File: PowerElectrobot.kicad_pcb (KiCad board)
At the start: 2 copper layers, 58 parts, among them J10 Conn_XT30F, J11 Conn_XT30F, J12 Conn_XT30F, J13 Conn_XT30F, J14 Conn_XT30F, J15 Conn_XT30F, J16 Conn_XT30F, J17 Conn_XT30F, J18 Conn_XT30F, J19 Conn_XT30F, J2 Conn_XT60M, J3 Conn_XT30F, J4 Conn_XT30F, J5 Conn_XT30F, J6 Conn_XT30F, J7 Conn_XT30F, J8 Conn_01x04, J9 Conn_01x04, Q1 BTS117, Q2 BTS117, Q3 BTS117, Q4 BTS117, Q5 BTS117, Q6 BTS117, Q7 BTS117, Q8 BTS117, U1 DSPIC33FJ128MC802-xSP, U2 TSR_2-2450, U3 MCP1804x-3302xDB, U4 ACS712xLCTR-05B, U5 ACS712xLCTR-05B, U6 ACS712xLCTR-20A

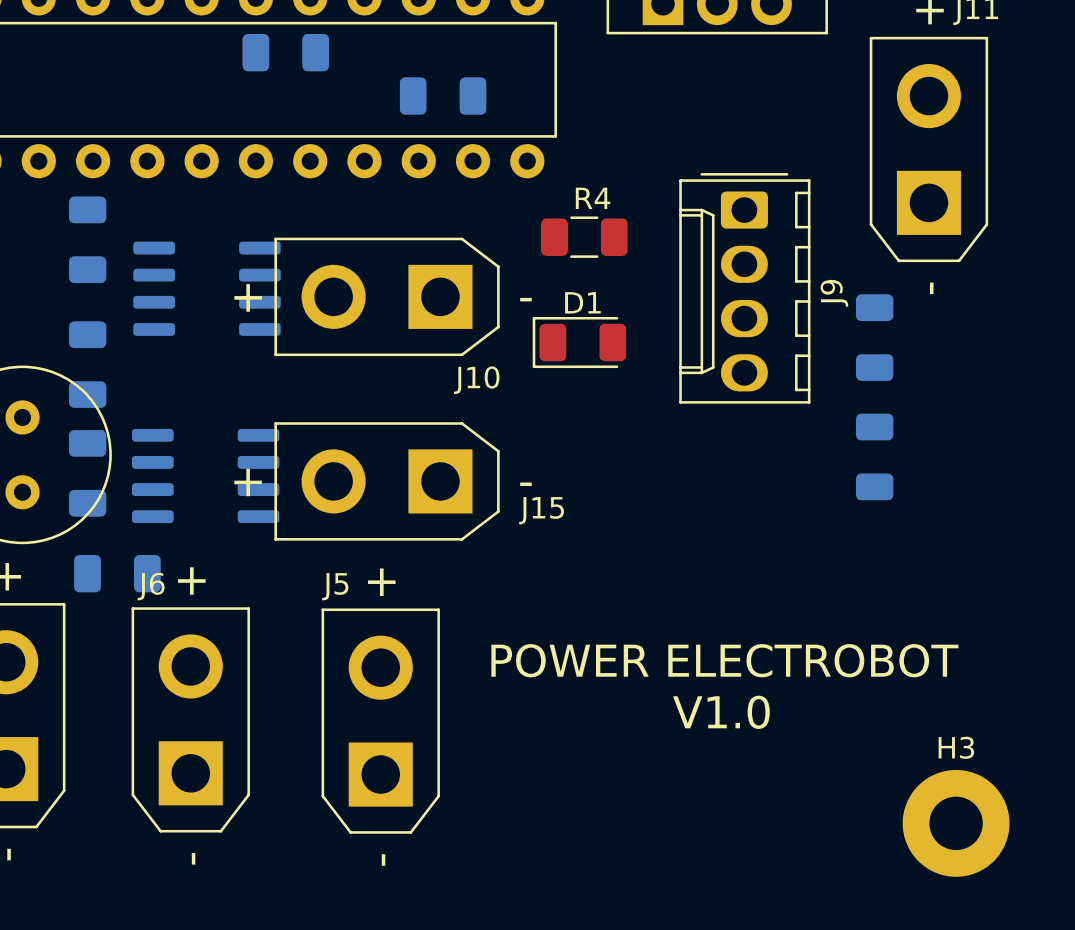
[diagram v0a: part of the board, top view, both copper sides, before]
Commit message: Création des via de 1.2mm
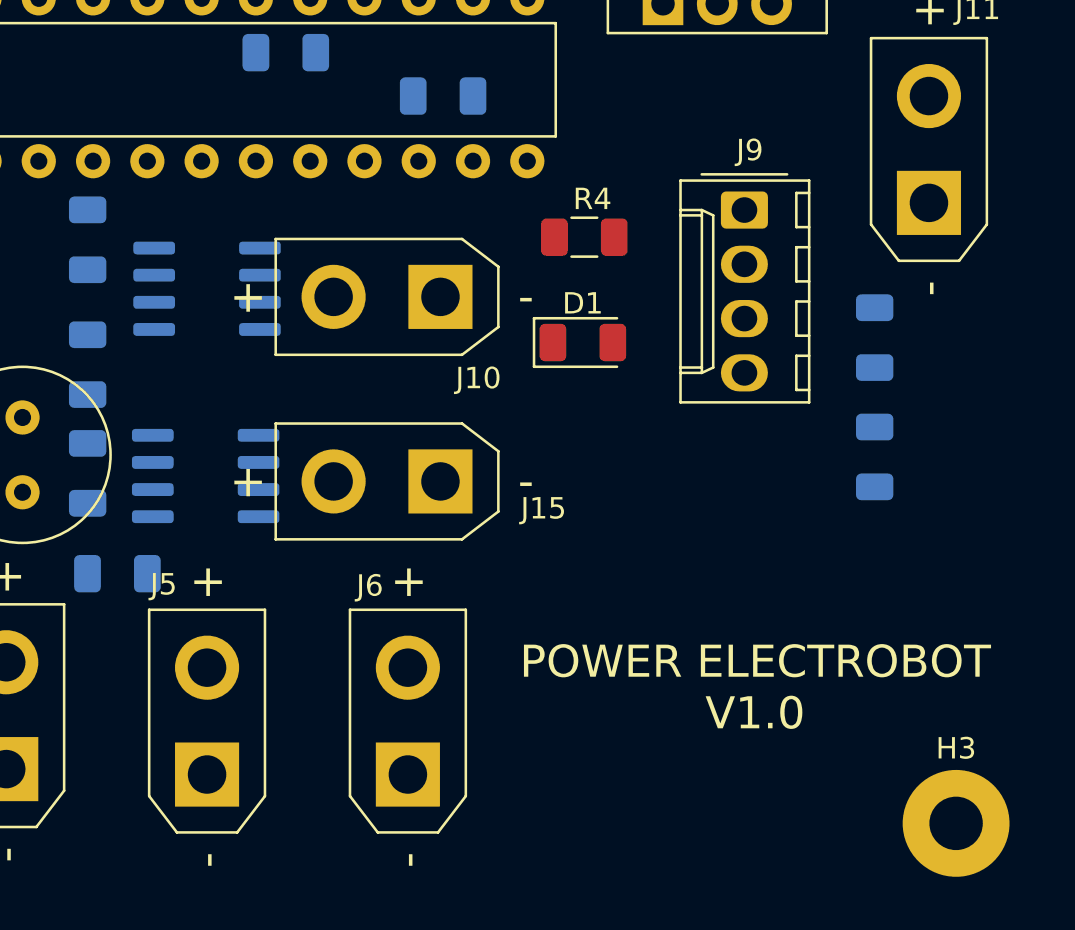
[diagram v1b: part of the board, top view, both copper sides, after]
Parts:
- moved J6 10.2 mm to (125.7, 117.6)
- moved J5 8.13 mm to (116.3, 117.6)
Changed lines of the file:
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@@
   )
   (setup
-    (last_trace_width 1.5)
+    (last_trace_width 0.25)
     (user_trace_width 0.5)
     (user_trace_width 0.75)
@@
     (user_trace_width 1.5)
     (user_trace_width 2)
+    (user_trace_width 2.5)
+    (user_trace_width 3)
     (trace_clearance 0.2)
     (zone_clearance 0.508)
@@
     (via_min_size 0.4)
     (via_min_drill 0.3)
+    (user_via 1.2 0.6)
     (uvia_size 0.3)
     (uvia_drill 0.1)
@@
   )
   (module XT30:AMASS_XT30UPB-F_1x02_P5.0mm_Vertical (layer F.Cu)
-    (at 124.46 117.602 90)
+    (at 116.332 117.602 90)
     (descr "Connector XT30 Vertical PCB Female, https://www.tme.eu/en/Document/4acc913878197f8c2e30d4b8cdc47230/XT30UPB%20SPEC.pdf")
     (tags "RC Connector XT30")
@@
   )
   (module XT30:AMASS_XT30UPB-F_1x02_P5.0mm_Vertical (layer F.Cu)
-    (at 115.57 117.545001 90)
+    (at 125.73 117.602 90)
     (descr "Connector XT30 Vertical PCB Female, https://www.tme.eu/en/Document/4acc913878197f8c2e30d4b8cdc47230/XT30UPB%20SPEC.pdf")
     (tags "RC Connector XT30")
@@
     (descr "Molex KK-254 Interconnect System, old/engineering part number: AE-6410-04A example for new part number: 22-27-2041, 4 Pins (http://www.molex.com/pdm_docs/sd/022272021_sd.pdf), generated with kicad-footprint-generator")
     (tags "connector Molex KK-254 side entry")
-    (fp_text reference J9 (at 3.81 -4.12 90) (layer F.SilkS)
+    (fp_text reference J9 (at -2.794 -0.254 180) (layer F.SilkS)
       (effects (font (size 1 1) (thickness 0.15)))
     )
@@
   (gr_circle (center 120.396 101.6) (end 120.523 101.6) (layer B.SilkS) (width 0.5))
   (gr_circle (center 120.396 92.964) (end 120.523 92.964) (layer B.SilkS) (width 0.5))
-  (gr_text "POWER ELECTROBOT\nV1.0" (at 140.462 113.538) (layer F.SilkS)
+  (gr_text "POWER ELECTROBOT\nV1.0" (at 141.986 113.538) (layer F.SilkS)
     (effects (font (size 1.5 1.5) (thickness 0.15)))
   )

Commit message: Début du routage de la carte
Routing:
- net /VBAT: track 0.00 -> 224.8 mm
- net +5V: track 0.00 -> 119.9 mm, vias 0 -> 2
- net GND: track 0.00 -> 90.1 mm, vias 0 -> 1
- net /3.3V_dsPIC: track 0.00 -> 87.9 mm, vias 0 -> 3
- net /MEAS_CURR_VBAT: track 0.00 -> 35.4 mm
- net Net-(J18-Pad1): track 0.00 -> 32.5 mm
- net Net-(J12-Pad1): track 0.00 -> 23.9 mm
- net /dsPIC_Stor8: track 0.00 -> 20.4 mm
- net Net-(J14-Pad1): track 0.00 -> 19.0 mm
- net /dsPIC_MCLR: track 0.00 -> 18.6 mm
- net Net-(J11-Pad1): track 0.00 -> 14.7 mm
- net /dsPIC_Stor7: track 0.00 -> 14.2 mm
- net /dsPIC_Stor2: track 0.00 -> 13.3 mm
- net Net-(J17-Pad1): track 0.00 -> 12.1 mm
- net Net-(J13-Pad1): track 0.00 -> 11.2 mm
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
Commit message: mise a jour pcb
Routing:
- net /dsPIC_PGED1: track 0.00 -> 23.1 mm, vias 0 -> 1
- net /VBAT: track 224.8 -> 239.1 mm
- net /MEAS_CURR_1: track 0.00 -> 11.0 mm
- net /I2C_SCL1: track 6.94 -> 17.6 mm, vias 0 -> 1
- net /VBAT_f: track 6.57 -> 15.7 mm
- net Net-(C10-Pad2): track 0.00 -> 3.74 mm
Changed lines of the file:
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@@
     (thickness 1.6)
     (drawings 3)
-    (tracks 266)
+    (tracks 297)
     (zones 0)
     (modules 58)
@@
   )
   (setup
-    (last_trace_width 0.75)
+    (last_trace_width 1)
     (user_trace_width 0.5)
     (user_trace_width 0.75)
@@
   (segment (start 103.124 92.514) (end 103.119001 92.509001) (width 0.75) (layer B.Cu) (net 3))
   (segment (start 103.124 95.25) (end 103.124 92.514) (width 0.75) (layer B.Cu) (net 3))
+  (segment (start 101.637999 88.100001) (end 100.838 88.9) (width 0.25) (layer B.Cu) (net 3))
+  (segment (start 101.963001 87.774999) (end 101.637999 88.100001) (width 0.25) (layer B.Cu) (net 3))
+  (segment (start 103.918001 87.774999) (end 101.963001 87.774999) (width 0.25) (layer B.Cu) (net 3))
+  (segment (start 104.503001 88.359999) (end 103.918001 87.774999) (width 0.25) (layer B.Cu) (net 3))
+  (segment (start 104.503001 90.305001) (end 104.503001 88.359999) (width 0.25) (layer B.Cu) (net 3))
+  (segment (start 103.119001 91.689001) (end 104.503001 90.305001) (width 0.25) (layer B.Cu) (net 3))
+  (segment (start 103.119001 92.509001) (end 103.119001 91.689001) (width 0.25) (layer B.Cu) (net 3))
   (segment (start 95.69171 85.15629) (end 94.996 85.852) (width 0.75) (layer B.Cu) (net 4))
   (segment (start 96.19201 84.65599) (end 95.69171 85.15629) (width 0.75) (layer B.Cu) (net 4))
@@
   (segment (start 116.332 112.602) (end 116.332 104.332) (width 0.75) (layer B.Cu) (net 5))
   (segment (start 116.332 104.332) (end 117.27201 103.39199) (width 0.75) (layer B.Cu) (net 5))
+  (segment (start 92.879999 97.261999) (end 97.431998 92.71) (width 1) (layer F.Cu) (net 5))
+  (segment (start 89.408 103.632) (end 92.879999 100.160001) (width 1) (layer F.Cu) (net 5))
+  (segment (start 92.879999 100.160001) (end 92.879999 97.261999) (width 1) (layer F.Cu) (net 5))
   (segment (start 106.56463 104.394) (end 107.696 104.394) (width 0.75) (layer B.Cu) (net 6))
   (segment (start 101.426 104.394) (end 106.56463 104.394) (width 0.75) (layer B.Cu) (net 6))
@@
   (segment (start 94.822 97.79) (end 99.822 102.79) (width 0.75) (layer F.Cu) (net 6))
   (segment (start 93.98 97.79) (end 94.822 97.79) (width 0.75) (layer F.Cu) (net 6))
+  (segment (start 112.262 95.504) (end 110.744 97.022) (width 0.25) (layer B.Cu) (net 7))
+  (segment (start 113.857 95.504) (end 112.262 95.504) (width 0.25) (layer B.Cu) (net 7))
   (segment (start 77.256195 108.585) (end 78.108 108.585) (width 0.75) (layer B.Cu) (net 9))
   (segment (start 78.108 108.585) (end 79.183 108.585) (width 0.75) (layer B.Cu) (net 9))
@@
   (segment (start 74.233 112.333) (end 76.708 114.808) (width 0.75) (layer B.Cu) (net 12))
   (segment (start 74.233 109.855) (end 74.233 112.333) (width 0.75) (layer B.Cu) (net 12))
+  (segment (start 87.884 90.852) (end 88.566 90.17) (width 0.25) (layer B.Cu) (net 14))
+  (segment (start 87.884 92.202) (end 87.884 90.852) (width 0.25) (layer B.Cu) (net 14))
+  (via (at 88.9 90.17) (size 0.8) (drill 0.4) (layers F.Cu B.Cu) (net 14))
+  (segment (start 88.566 90.17) (end 88.9 90.17) (width 0.25) (layer B.Cu) (net 14))
+  (segment (start 105.118001 88.100001) (end 105.918 88.9) (width 0.25) (layer F.Cu) (net 14))
+  (segment (start 102.423981 85.405981) (end 105.118001 88.100001) (width 0.25) (layer F.Cu) (net 14))
+  (segment (start 93.664019 85.405981) (end 102.423981 85.405981) (width 0.25) (layer F.Cu) (net 14))
+  (segment (start 88.9 90.17) (end 93.664019 85.405981) (width 0.25) (layer F.Cu) (net 14))
   (segment (start 98.298 89.141552) (end 98.298 88.9) (width 0.75) (layer B.Cu) (net 15))
   (segment (start 93.562542 93.87701) (end 98.298 89.141552) (width 0.75) (layer B.Cu) (net 15))
@@
   (segment (start 143.51 95.758) (end 141.478 93.726) (width 0.75) (layer B.Cu) (net 16))
   (segment (start 147.574 95.758) (end 143.51 95.758) (width 0.75) (layer B.Cu) (net 16))
+  (segment (start 126.238 82.41137) (end 128.91663 85.09) (width 1) (layer F.Cu) (net 16))
+  (segment (start 126.238 81.28) (end 126.238 82.41137) (width 1) (layer F.Cu) (net 16))
+  (segment (start 128.91663 85.09) (end 134.62 85.09) (width 1) (layer F.Cu) (net 16))
+  (via (at 134.62 85.09) (size 0.8) (drill 0.4) (layers F.Cu B.Cu) (net 16))
   (segment (start 141.708 96.266) (end 141.478 96.266) (width 0.75) (layer B.Cu) (net 17))
   (segment (start 146.12399 100.68199) (end 141.708 96.266) (width 0.75) (layer B.Cu) (net 17))
@@
   (segment (start 80.258 109.855) (end 81.09999 109.01301) (width 0.75) (layer B.Cu) (net 37))
   (segment (start 79.183 109.855) (end 80.258 109.855) (width 0.75) (layer B.Cu) (net 37))
+  (segment (start 110.198001 89.699999) (end 110.998 88.9) (width 0.25) (layer B.Cu) (net 38))
+  (segment (start 109.54399 90.35401) (end 110.198001 89.699999) (width 0.25) (layer B.Cu) (net 38))
+  (segment (start 109.54399 94.59318) (end 109.54399 90.35401) (width 0.25) (layer B.Cu) (net 38))
+  (segment (start 109.88082 94.93001) (end 109.54399 94.59318) (width 0.25) (layer B.Cu) (net 38))
+  (segment (start 111.60718 94.93001) (end 109.88082 94.93001) (width 0.25) (layer B.Cu) (net 38))
+  (segment (start 112.30319 94.234) (end 111.60718 94.93001) (width 0.25) (layer B.Cu) (net 38))
+  (segment (start 113.857 94.234) (end 112.30319 94.234) (width 0.25) (layer B.Cu) (net 38))
   (segment (start 112.24199 101.276688) (end 112.666688 100.85199) (width 0.75) (layer B.Cu) (net 39))
   (segment (start 112.24199 102.177312) (end 112.24199 101.276688) (width 0.75) (layer B.Cu) (net 39))

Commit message: Version initiale du placement de composants
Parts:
- added D2: LED, LED_SMD:LED_1206_3216Metric, F.Cu at (147.0, 90.0)
- added D3: LED, LED_SMD:LED_1206_3216Metric, F.Cu at (129.0, 65.6)
- added D4: LED, LED_SMD:LED_1206_3216Metric, F.Cu at (147.1, 75.3)
- added D5: LED, LED_SMD:LED_1206_3216Metric, F.Cu at (114.1, 65.6)
- added D6: LED, LED_SMD:LED_1206_3216Metric, F.Cu at (136.2, 76.3)
- added D7: LED, LED_SMD:LED_1206_3216Metric, F.Cu at (99.9, 65.7)
- added D8: LED, LED_SMD:LED_1206_3216Metric, F.Cu at (143.8, 65.7)
- added D9: LED, LED_SMD:LED_1206_3216Metric, F.Cu at (85.4, 65.7)
- added R10: 91k, Resistor_SMD:R_1206_3216Metric, F.Cu at (116.0, 92.4)
- added R11: 47k, Resistor_SMD:R_1206_3216Metric, F.Cu at (115.8, 101.2)
- added R12: 91k, Resistor_SMD:R_1206_3216Metric, F.Cu at (115.9, 103.9)
- added R13: R, Resistor_SMD:R_1206_3216Metric, F.Cu at (147.1, 85.1)
- added R14: R, Resistor_SMD:R_1206_3216Metric, F.Cu at (123.4, 65.6)
- added R15: R, Resistor_SMD:R_1206_3216Metric, F.Cu at (147.1, 70.3)
- added R16: R, Resistor_SMD:R_1206_3216Metric, F.Cu at (108.7, 65.6)
- added R17: R, Resistor_SMD:R_1206_3216Metric, B.Cu at (134.5, 71.1)
- added R18: R, Resistor_SMD:R_1206_3216Metric, F.Cu at (94.4, 65.8)
- added R19: R, Resistor_SMD:R_1206_3216Metric, F.Cu at (138.4, 65.7)
- added R20: R, Resistor_SMD:R_1206_3216Metric, F.Cu at (79.7, 65.7)
- added R7: 47k, Resistor_SMD:R_1206_3216Metric, F.Cu at (104.1, 94.4)
- added R8: 91k, Resistor_SMD:R_1206_3216Metric, F.Cu at (104.1, 91.8)
- added R9: 47k, Resistor_SMD:R_1206_3216Metric, F.Cu at (116.0, 95.1)
- C8: value 1u -> 47u
- R4: value 4.7k -> 470
- moved H2 2.27 mm to (152.0, 59.0)
- moved H1 2.18 mm to (72.9, 59.0)
- moved J12 1.88 mm to (129.3, 61.1)
- moved J14 1.88 mm to (114.6, 61.1)
- moved J17 1.88 mm to (100.1, 61.1)
- moved J18 1.88 mm to (144.3, 61.1)
- moved J19 1.88 mm to (85.8, 61.1)
- moved J11 1.68 mm to (151.8, 90.9)
- moved J13 1.68 mm to (151.8, 76.1)
- moved J7 1.02 mm to (98.8, 97.8)
- moved H3 0.74 mm to (152.0, 120.3)
- moved H4 0.41 mm to (72.9, 120.3)
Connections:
- U4 pad 7: /MEAS_CURR_1 -> Net-(R9-Pad2)
- U5 pad 7: /MEAS_CURR_2 -> Net-(R11-Pad2)
- U6 pad 7: /MEAS_CURR_VBAT -> Net-(R7-Pad2)
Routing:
- net /VBAT: track 239.1 -> 0.00 mm
- net +5V: track 119.9 -> 0.00 mm, vias 2 -> 0
- net GND: track 90.1 -> 0.00 mm, vias 1 -> 0
- net /3.3V_dsPIC: track 87.9 -> 0.00 mm, vias 3 -> 0
- net /MEAS_CURR_VBAT: track 35.4 -> 0.00 mm
- net Net-(D8-Pad1): track 32.5 -> 0.00 mm
- net Net-(D3-Pad1): track 23.9 -> 0.00 mm
- net /dsPIC_PGED1: track 23.1 -> 0.00 mm, vias 1 -> 0
- net /dsPIC_Stor8: track 20.4 -> 0.00 mm
- net Net-(D5-Pad1): track 19.0 -> 0.00 mm
- net /dsPIC_MCLR: track 18.6 -> 0.00 mm
- net /I2C_SCL1: track 17.6 -> 0.00 mm, vias 1 -> 0
- net /VBAT_f: track 15.7 -> 0.00 mm
- net Net-(D2-Pad1): track 14.7 -> 0.00 mm
- net /dsPIC_Stor7: track 14.2 -> 0.00 mm
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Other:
- board outline added: 87.4 x 68.1 mm

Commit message: Version initiale du routage
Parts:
- moved R6 29.7 mm to (123.7, 85.0), turned to 270 degrees
- moved R5 24.4 mm to (126.4, 85.0)
- moved C3 2.07 mm to (129.3, 85.0), turned to 90 degrees
- moved C1 1.88 mm to (118.6, 85.0), turned to 270 degrees
- moved R9 1.27 mm to (114.9, 95.8)
- moved C13 1.14 mm to (83.7, 109.5)
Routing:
- net /VBAT: track 0.00 -> 347.7 mm
- net +5V: track 0.00 -> 146.9 mm
- net /3.3V_dsPIC: track 0.00 -> 61.6 mm
- net GND: track 0.00 -> 51.8 mm, vias 0 -> 3
- net Net-(D8-Pad1): track 0.00 -> 41.1 mm
- net Net-(R7-Pad2): track 0.00 -> 38.3 mm, vias 0 -> 1
- net Net-(D3-Pad1): track 0.00 -> 29.3 mm
- net /I2C_SDA1: track 0.00 -> 28.7 mm
- net /I2C_SCL1: track 0.00 -> 24.8 mm
- net /dsPIC_PGED1: track 0.00 -> 24.6 mm, vias 0 -> 1
- net Net-(D5-Pad1): track 0.00 -> 23.7 mm
- net /dsPIC_PGEC1: track 0.00 -> 22.7 mm
- net /MEAS_CURR_2: track 0.00 -> 21.4 mm
- net /dsPIC_Stor8: track 0.00 -> 19.9 mm
- net Net-(D2-Pad1): track 0.00 -> 18.9 mm
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- added copper zone on B.Cu, net GND
- added copper zone on F.Cu, net GND
